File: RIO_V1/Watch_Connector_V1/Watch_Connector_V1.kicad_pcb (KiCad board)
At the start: 2 copper layers, 16.1 x 18.7 mm, 2 parts, among them J1 Conn_01x04_Socket, J2 POGO_Connector

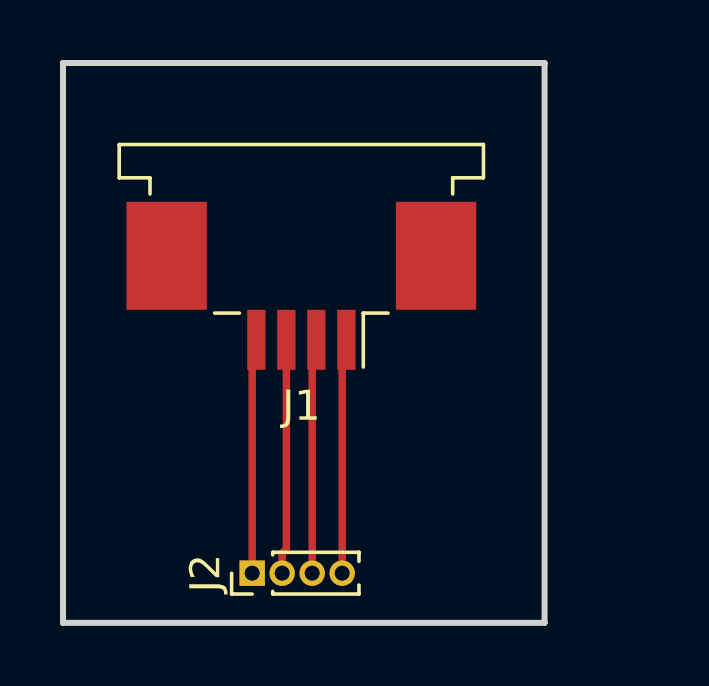
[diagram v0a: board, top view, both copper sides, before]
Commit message: Changed The FPC Connector To A Smaller Pitch
Changed the FPC connector on the PCB so that the pitch is reduced and overall footprint is minimized as much as possible
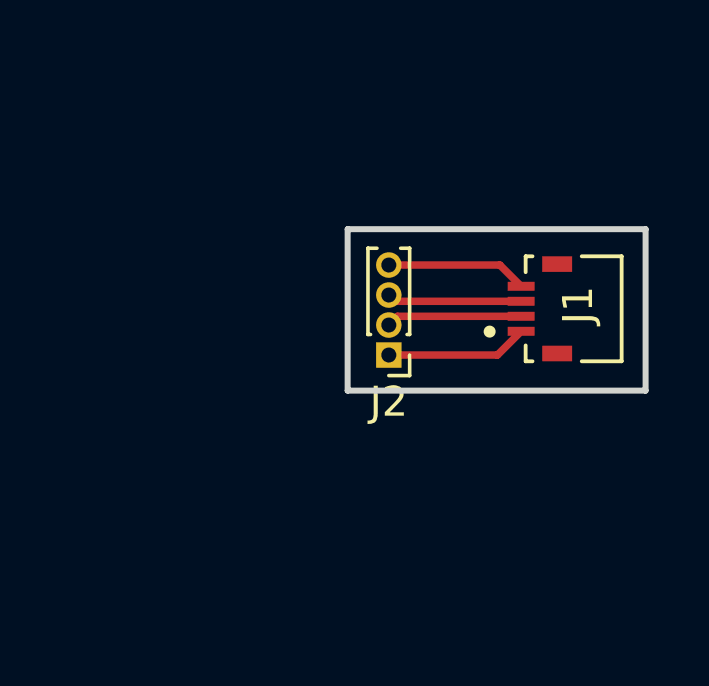
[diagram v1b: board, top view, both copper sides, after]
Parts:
- J1: value Conn_01x04_Socket -> 59453-042110ECHLF; footprint Connector_FFC-FPC:TE_84952-4_1x04-1MP_P1.0mm_Horizontal -> Connector:AMPHENOL_59453-042110ECHLF
- J2: value POGO_Connector -> Conn_01x04_Pin
- moved J2 8.58 mm to (146.7, 103.2), turned to 180 degrees
- moved J1 8.56 mm to (152.3, 101.7), turned to 90 degrees
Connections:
- J1 pad 1: Net-(J1-Pin_1) -> Net-(J2-Pin_1)
- J1 pad 2: Net-(J1-Pin_2) -> Net-(J2-Pin_2)
- J1 pad 3: Net-(J1-Pin_3) -> Net-(J2-Pin_3)
- J1 pad 4: Net-(J1-Pin_4) -> Net-(J2-Pin_4)
- J2 pad 1: Net-(J1-Pin_4) -> Net-(J2-Pin_1)
- J2 pad 2: Net-(J1-Pin_3) -> Net-(J2-Pin_2)
- J2 pad 3: Net-(J1-Pin_2) -> Net-(J2-Pin_3)
- J2 pad 4: Net-(J1-Pin_1) -> Net-(J2-Pin_4)
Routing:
- net Net-(J1-Pin_4): track 7.84 -> 0.00 mm
- net Net-(J1-Pin_3): track 7.84 -> 0.00 mm
- net Net-(J1-Pin_2): track 7.84 -> 0.00 mm
- net Net-(J1-Pin_1): track 7.84 -> 0.00 mm
- net Net-(J2-Pin_1): track 0.00 -> 4.74 mm
- net Net-(J2-Pin_4): track 0.00 -> 4.70 mm
- net Net-(J2-Pin_2): track 0.00 -> 4.53 mm
- net Net-(J2-Pin_3): track 0.00 -> 4.50 mm
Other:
- board size 16.1 x 18.7 mm -> 9.9 x 5.4 mm
